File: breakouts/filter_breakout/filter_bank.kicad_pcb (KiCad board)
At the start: 4 copper layers, 34 parts, among them P1 CONN_01X05, U1 CONN_SMA, U2 HMC321, U3 HMC321, U4 CONN_SMA, U5 mounting_box

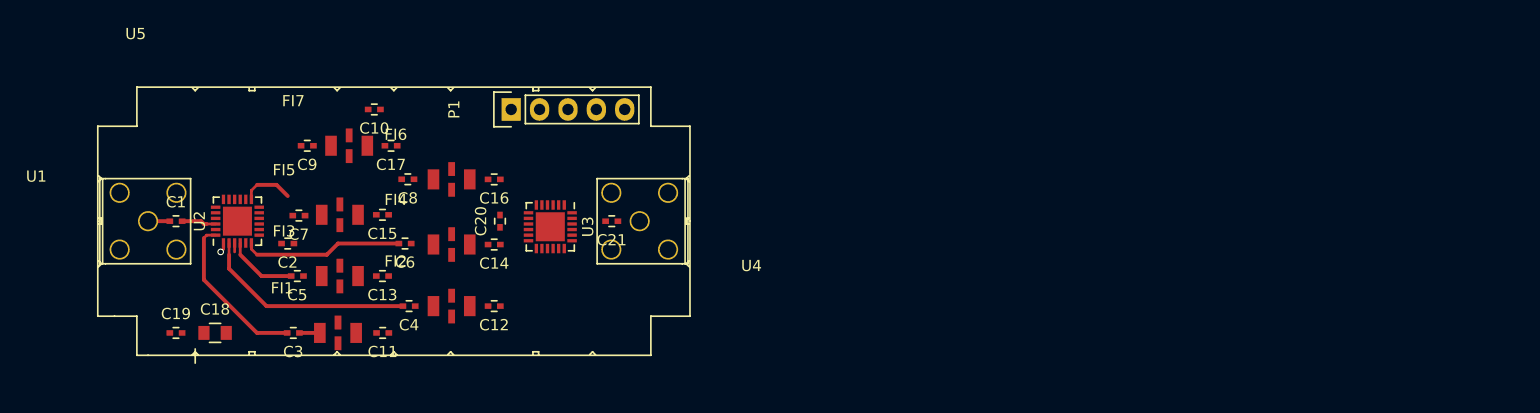
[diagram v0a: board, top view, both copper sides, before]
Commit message: layout of splitter, switch, and filter
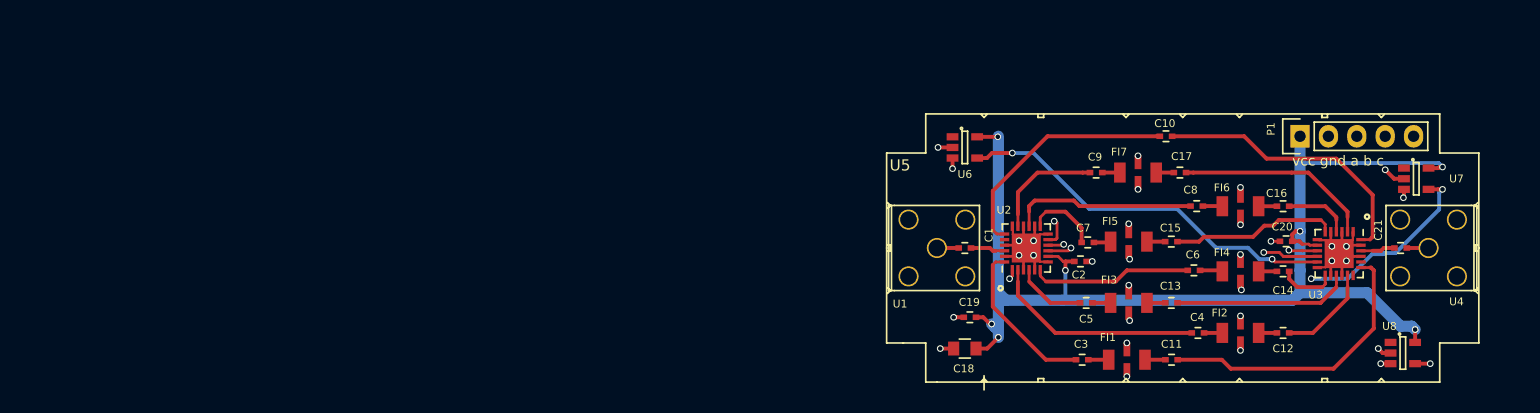
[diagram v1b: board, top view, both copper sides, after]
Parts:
- added U6: 74xx1G14, TO_SOT_Packages_SMD:SOT-23-5, F.Cu at (199.6, 98.4)
- added U7: 74xx1G14, TO_SOT_Packages_SMD:SOT-23-5, F.Cu at (240.0, 101.2)
- added U8: 74xx1G14, TO_SOT_Packages_SMD:SOT-23-5, F.Cu at (238.8, 116.8)
- moved C19 71.1 mm to (200.1, 113.6)
- moved C2 71.0 mm to (209.9, 108.6)
- moved C10 70.9 mm to (217.6, 97.4)
- moved C12 70.6 mm to (228.1, 115.0)
- moved C13 70.6 mm to (218.1, 112.3)
- moved C14 70.6 mm to (228.1, 109.5)
- moved C15 70.6 mm to (218.1, 106.8)
- moved C16 70.6 mm to (228.1, 103.7)
- moved FI2 70.6 mm to (224.3, 115.0)
- moved FI3 70.6 mm to (214.3, 112.3)
- moved FI4 70.6 mm to (224.3, 109.5)
- moved FI5 70.6 mm to (214.3, 106.8)
- moved FI6 70.6 mm to (224.3, 103.7)
- moved C1 70.6 mm to (199.6, 107.4)
- moved C11 70.6 mm to (218.1, 117.4)
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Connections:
- C10 pad 1: /RF8_O -> /RF1_O
- C11 pad 1: /RF1_O -> /RF8_O
- C12 pad 1: /RF2_O -> /RF7_O
- C13 pad 1: /RF3_O -> /RF6_O
- C14 pad 1: /RF4_O -> /RF5_O
- C15 pad 1: /RF5_O -> /RF4_O
- C16 pad 1: /RF6_O -> /RF3_O
- C17 pad 1: /RF7_O -> /RF2_O
- U2 pad 9: /CTLB -> /CTLC
- U3 pad 10: /CTLB -> /~CTLB
- U3 pad 11: /CTLA -> /~CTLA
- U3 pad 9: /CTLC -> /~CTLC
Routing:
- net VDD: track 0.00 -> 103.0 mm, vias 0 -> 7
- net /CTLC: track 0.00 -> 53.8 mm, vias 0 -> 2
- net /CTLA: track 0.00 -> 53.0 mm, vias 0 -> 2
- net GND: track 1.70 -> 42.7 mm, vias 1 -> 30
- net /CTLB: track 0.00 -> 40.0 mm, vias 0 -> 2
- net /~CTLA: track 0.00 -> 34.7 mm, vias 0 -> 2
- net /~CTLB: track 0.00 -> 30.9 mm, vias 0 -> 3
- net /~CTLC: track 0.00 -> 30.3 mm, vias 0 -> 2
- net /RF8_O: track 0.00 -> 25.8 mm
- net /RF1_O: track 0.00 -> 25.0 mm
- net /RF8_I: track 0.00 -> 21.8 mm
- net /RF2_O: track 0.00 -> 17.7 mm
- net /RF6_I: track 0.00 -> 16.7 mm
- net /RF6_O: track 0.00 -> 15.9 mm
- net /RF4_O: track 0.00 -> 14.8 mm
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- added copper zone on In1.Cu, net GND
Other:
- net class Default: clearance 0.2 -> 0.127; trace_width 0.25 -> 0.254
- rule trace_clearance: 0.2 -> 0.127
- board text added: "vcc gnd a b c"

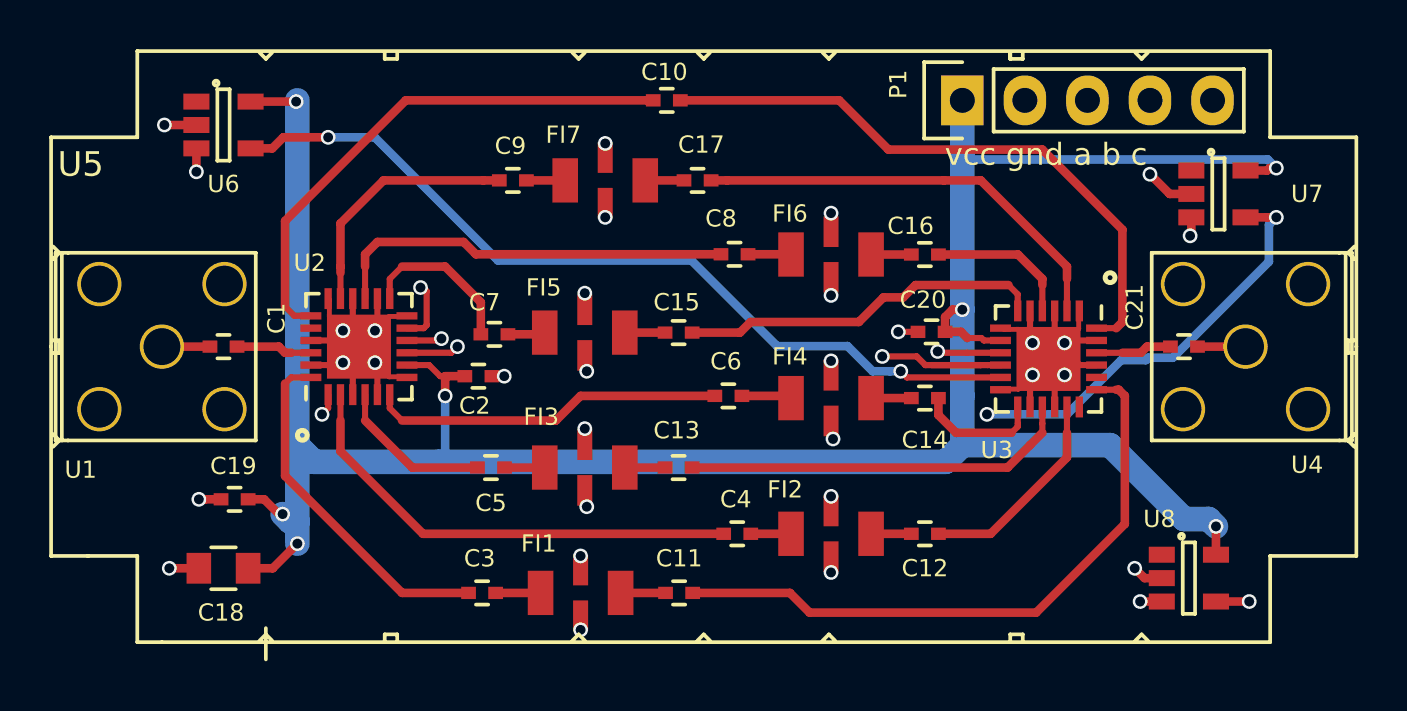
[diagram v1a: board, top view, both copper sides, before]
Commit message: started variable attenuator, revised synth, and added power splittert to detect board
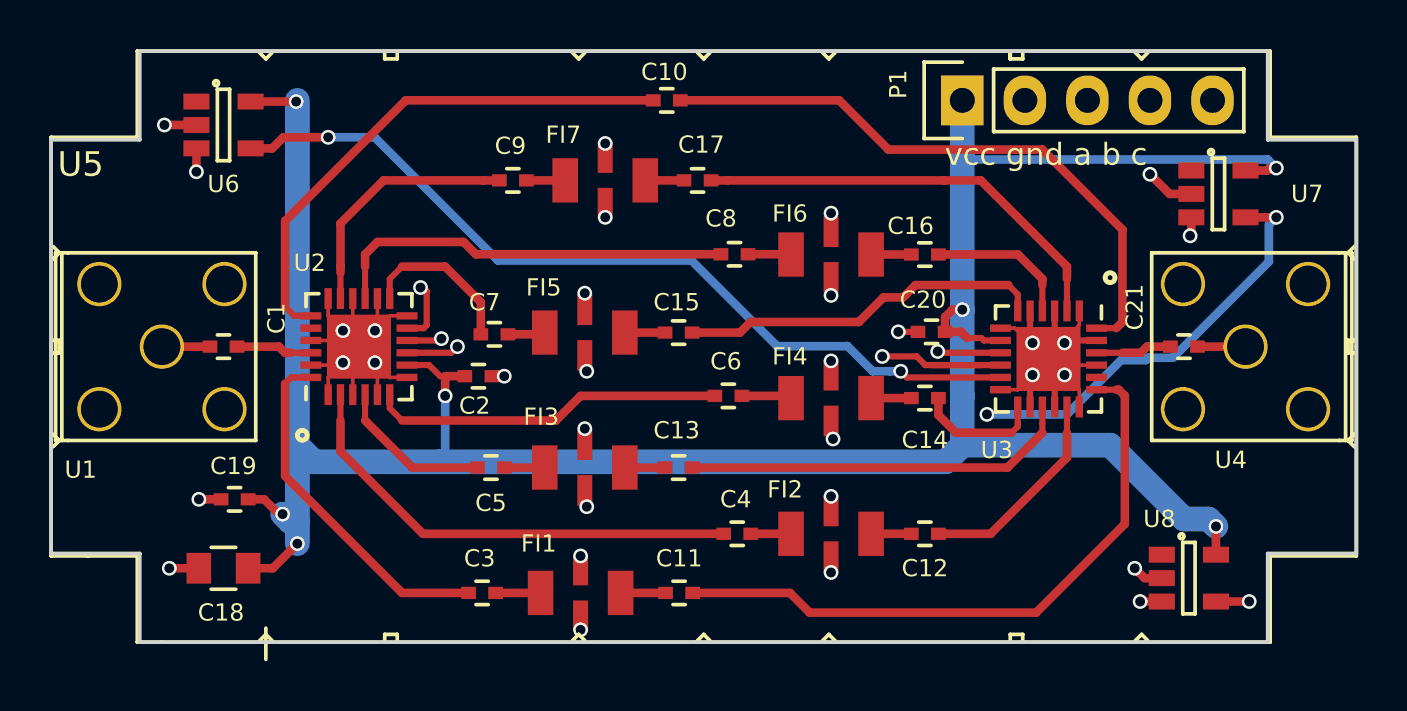
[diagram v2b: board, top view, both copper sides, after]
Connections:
- U4 pad 5: Net-(U4-Pad5) -> GND
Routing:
- net GND: track 42.7 -> 60.3 mm, vias 30 -> 29
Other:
- board outline added: 53 x 24 mm
- rule trace_min: 0.2 -> 0.15
- board text added: "filter bank r0"

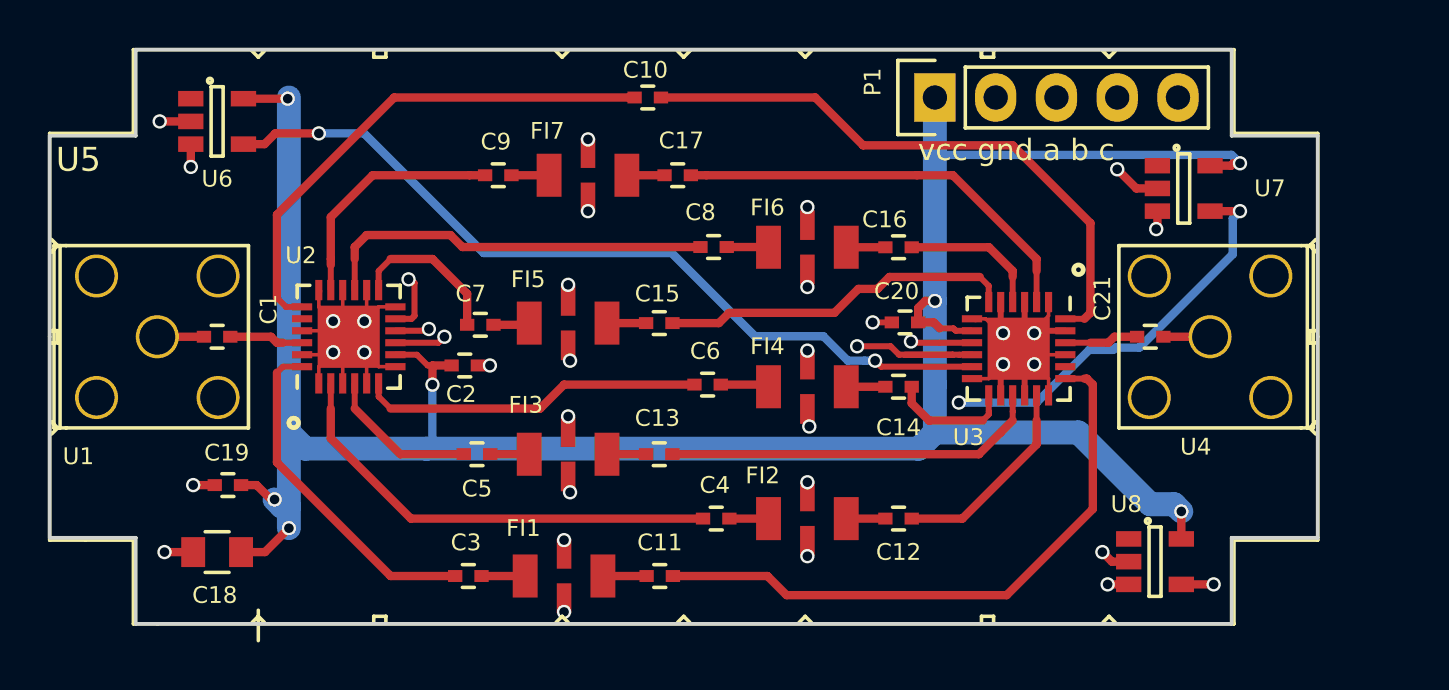
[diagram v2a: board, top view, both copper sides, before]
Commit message: trimmed ground plane on some breakouts so it doesn't disappear during panelization..
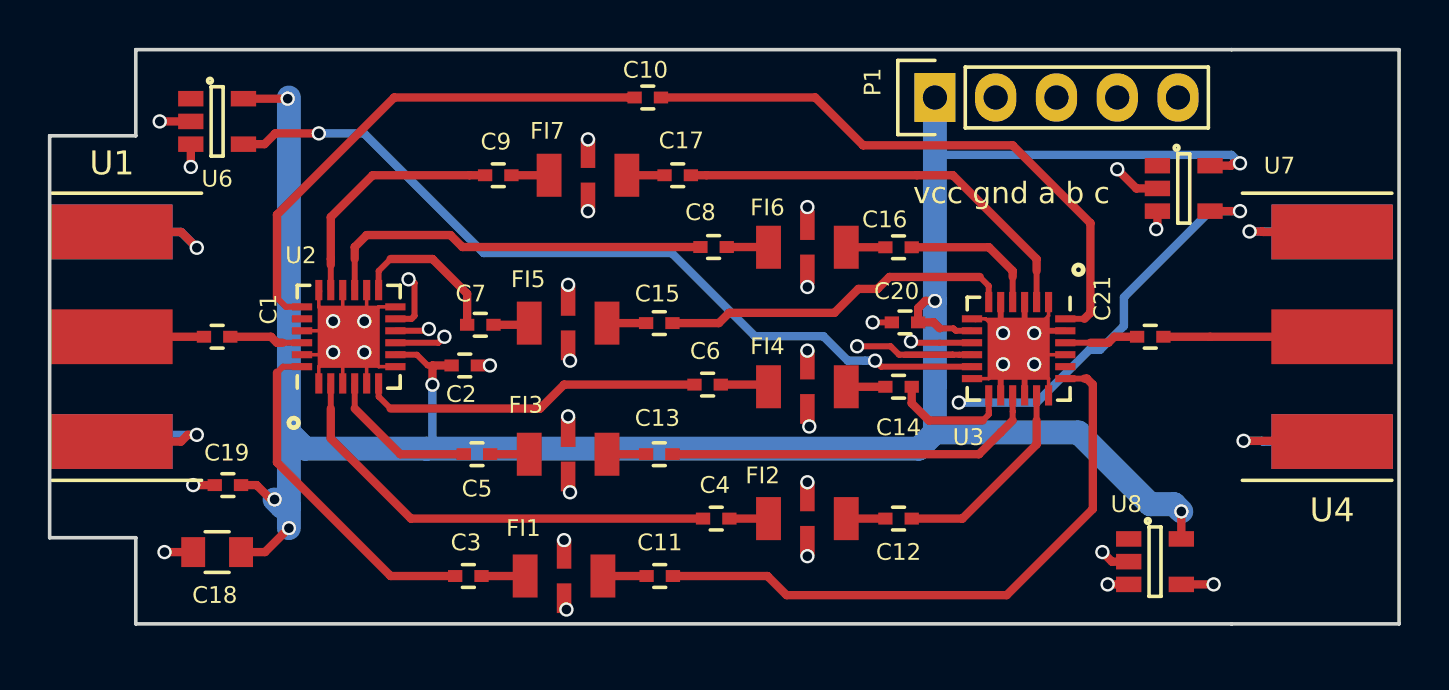
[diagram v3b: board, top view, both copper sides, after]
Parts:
- removed U5: mounting_box, vna_footprints:POMONA_2400BOX
- U1, U4: footprint vna_footprints:732512200_SMA -> vna_footprints:732511150_sma
- moved U4 5.10 mm to (246.2, 107.4), turned to 90 degrees
- moved U1 1.90 mm to (195.2, 107.4), turned to 270 degrees
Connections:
- U2 pad 20: Net-(U2-Pad20) -> (no net)
- U3 pad 20: Net-(U3-Pad20) -> (no net)
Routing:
- net GND: track 60.3 -> 85.8 mm, vias 29 -> 33
- net Net-(C21-Pad1): track 1.95 -> 7.05 mm
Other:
- board size 53 x 24 mm -> 56.4 x 24 mm
